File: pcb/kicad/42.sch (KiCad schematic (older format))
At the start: 92 parts, among them J1 USB_C_Receptacle, J2 USB_C_Receptacle, J3 USB_C_Receptacle, K1 KEYSW, K10 KEYSW, K11 KEYSW, K12 KEYSW, K13 KEYSW, K14 KEYSW, K15 KEYSW, K16 KEYSW, K17 KEYSW, K18 KEYSW, K19 KEYSW, K2 KEYSW, K20 KEYSW, K21 KEYSW, K22 KEYSW, K23 KEYSW, K24 KEYSW, K25 KEYSW, K26 KEYSW, K27 KEYSW, K28 KEYSW, K29 KEYSW, K3 KEYSW, K30 KEYSW, K31 KEYSW, K32 KEYSW, K33 KEYSW, K34 KEYSW, K35 KEYSW, K36 KEYSW, K37 KEYSW, K38 KEYSW, K39 KEYSW, K4 KEYSW, K40 KEYSW, K41 KEYSW, K42 KEYSW, K5 KEYSW, K6 KEYSW, K7 KEYSW, K8 KEYSW, K9 KEYSW, U1 TEENSY2.0

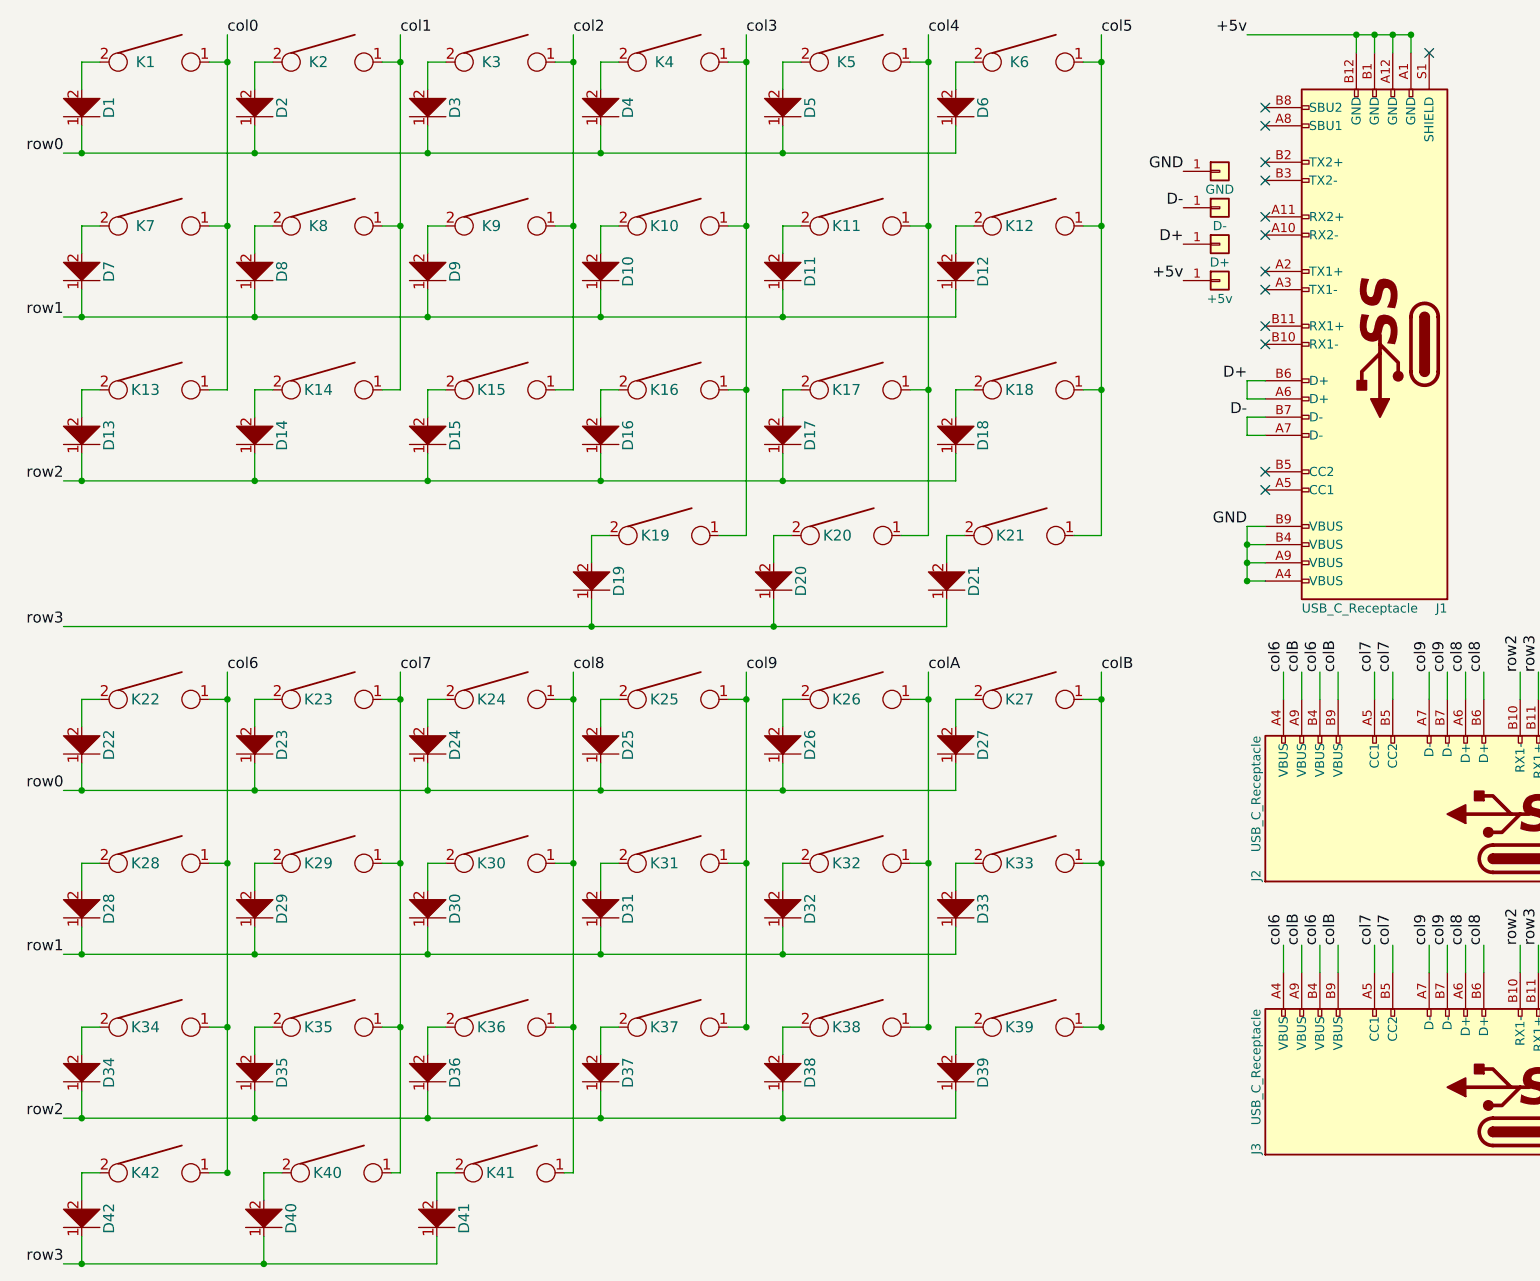
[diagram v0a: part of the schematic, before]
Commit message: fixed inverted connections on USB receptacle
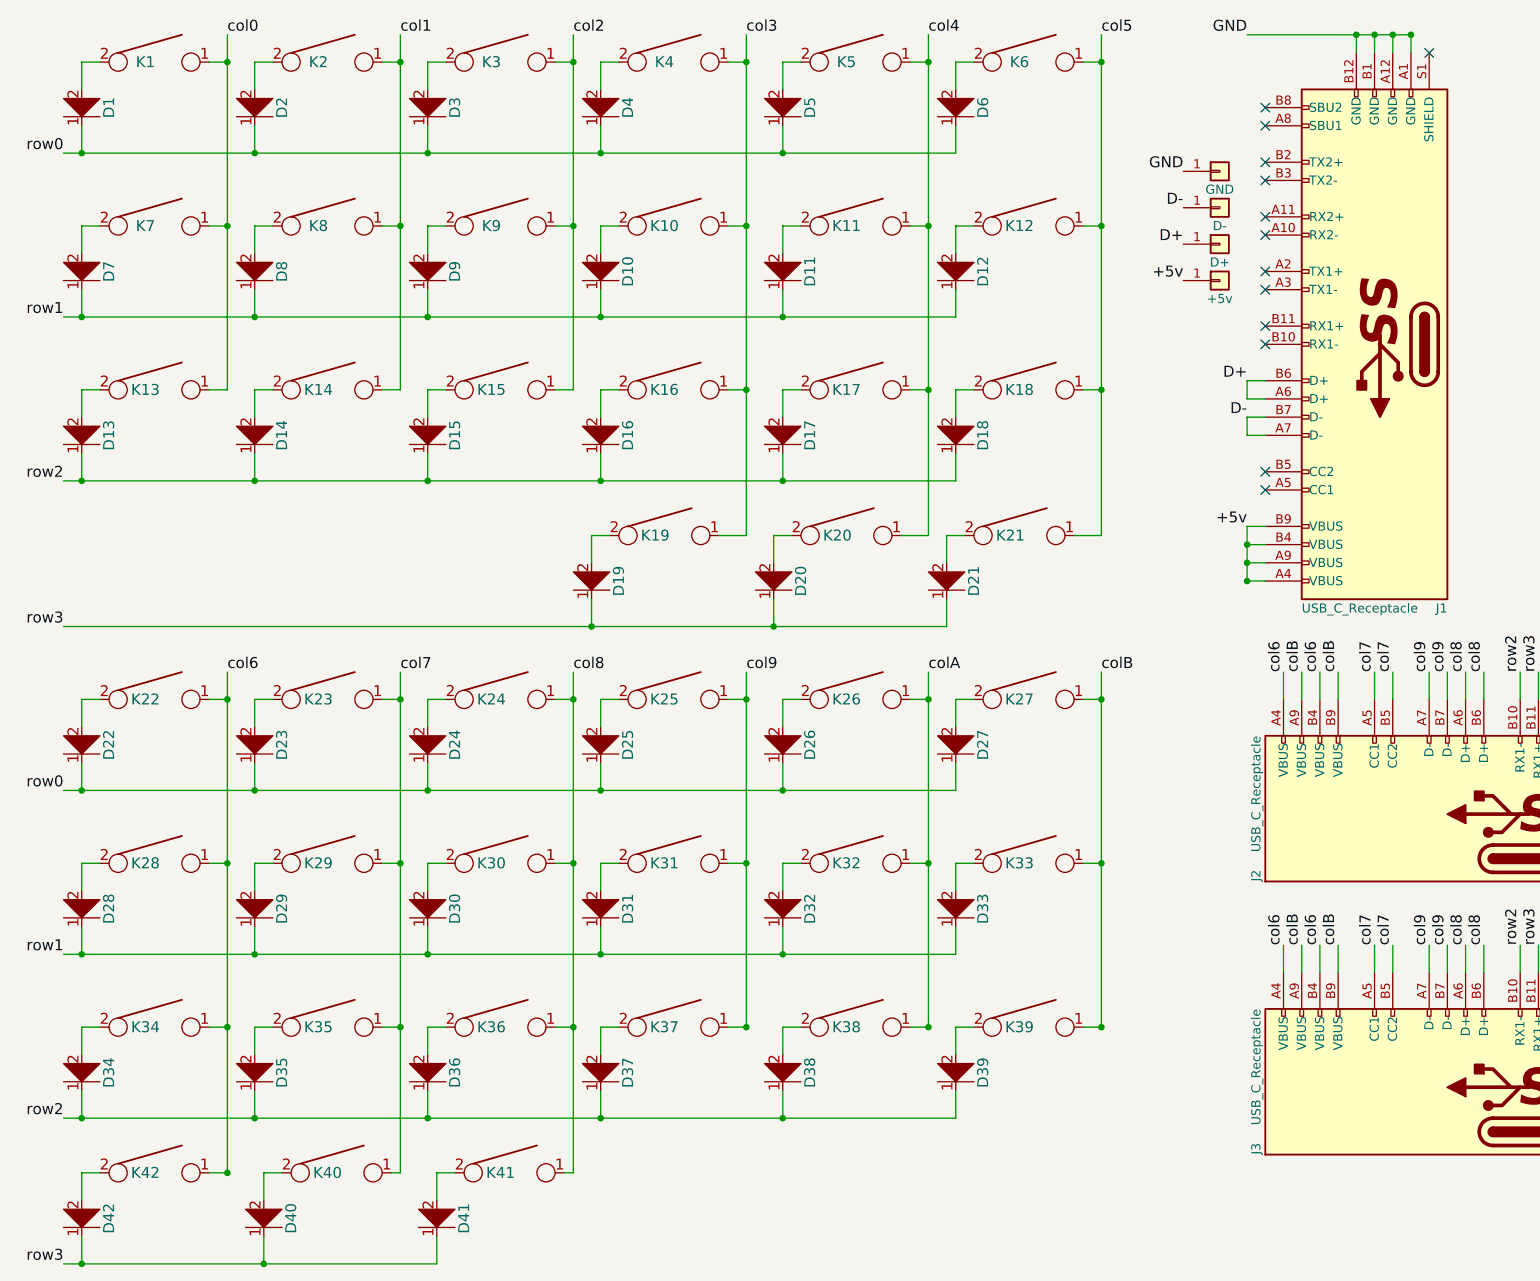
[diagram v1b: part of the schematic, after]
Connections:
- net +5v: now also J1.A4 (VBUS), J1.A9 (VBUS), J1.B4 (VBUS), J1.B9 (VBUS); no longer J1.A1 (GND), J1.A12 (GND), J1.B1 (GND), J1.B12 (GND)
- net GND: now also J1.A1 (GND), J1.A12 (GND), J1.B1 (GND), J1.B12 (GND); no longer J1.A4 (VBUS), J1.A9 (VBUS), J1.B4 (VBUS), J1.B9 (VBUS)
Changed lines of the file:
@@
 EESchema Schematic File Version 2
 LIBS:power
-LIBS:device
-LIBS:switches
-LIBS:relays
-LIBS:motors
-LIBS:transistors
-LIBS:conn
-LIBS:linear
-LIBS:regul
-LIBS:74xx
-LIBS:cmos4000
-LIBS:adc-dac
-LIBS:memory
-LIBS:xilinx
-LIBS:microcontrollers
-LIBS:dsp
-LIBS:microchip
-LIBS:analog_switches
-LIBS:motorola
-LIBS:texas
-LIBS:intel
-LIBS:audio
-LIBS:interface
-LIBS:digital-audio
-LIBS:philips
-LIBS:display
-LIBS:cypress
-LIBS:siliconi
-LIBS:opto
-LIBS:atmel
-LIBS:contrib
-LIBS:valves
-LIBS:42keyboard-cache
+LIBS:42-cache
 EELAYER 25 0
 EELAYER END
@@
 	1050 1250 1050 1400
 Wire Wire Line
-	950  1400 1050 1400
-Wire Wire Line
-	1050 1400 2000 1400
-Wire Wire Line
-	2000 1400 2950 1400
-Wire Wire Line
-	2950 1400 3900 1400
-Wire Wire Line
-	3900 1400 4900 1400
-Wire Wire Line
-	4900 1400 5850 1400
+	950  1400 5850 1400
 Wire Wire Line
 	2000 1400 2000 1250
@@
 	1050 2150 1050 2300
 Wire Wire Line
-	950  2300 1050 2300
-Wire Wire Line
-	1050 2300 2000 2300
-Wire Wire Line
-	2000 2300 2950 2300
-Wire Wire Line
-	2950 2300 3900 2300
-Wire Wire Line
-	3900 2300 4900 2300
-Wire Wire Line
-	4900 2300 5850 2300
+	950  2300 5850 2300
 Wire Wire Line
 	2000 2300 2000 2150
@@
 	1050 3050 1050 3200
 Wire Wire Line
-	950  3200 1050 3200
-Wire Wire Line
-	1050 3200 2000 3200
-Wire Wire Line
-	2000 3200 2950 3200
-Wire Wire Line
-	2950 3200 3900 3200
-Wire Wire Line
-	3900 3200 4900 3200
-Wire Wire Line
-	4900 3200 5850 3200
+	950  3200 5850 3200
 Wire Wire Line
 	2000 3200 2000 3050
@@
 	1750 900  1850 900
 Wire Wire Line
-	1850 750  1850 900
-Wire Wire Line
-	1850 900  1850 1800
-Wire Wire Line
-	1850 1800 1850 2700
+	1850 750  1850 2700
 Wire Wire Line
 	1850 2700 1750 2700
@@
 	2700 900  2800 900
 Wire Wire Line
-	2800 750  2800 900
-Wire Wire Line
-	2800 900  2800 1800
-Wire Wire Line
-	2800 1800 2800 2700
+	2800 750  2800 2700
 Wire Wire Line
 	2800 2700 2700 2700
@@
 	3650 900  3750 900
 Wire Wire Line
-	3750 750  3750 900
-Wire Wire Line
-	3750 900  3750 1800
-Wire Wire Line
-	3750 1800 3750 2700
+	3750 750  3750 2700
 Wire Wire Line
 	3750 2700 3650 2700
@@
 	4600 900  4700 900
 Wire Wire Line
-	4700 750  4700 900
-Wire Wire Line
-	4700 900  4700 1800
-Wire Wire Line
-	4700 1800 4700 2700
-Wire Wire Line
-	4700 2700 4700 3500
+	4700 750  4700 3500
 Wire Wire Line
 	4700 2700 4600 2700
@@
 	5600 900  5700 900
 Wire Wire Line
-	5700 750  5700 900
-Wire Wire Line
-	5700 900  5700 1800
-Wire Wire Line
-	5700 1800 5700 2700
-Wire Wire Line
-	5700 2700 5700 3500
+	5700 750  5700 3500
 Wire Wire Line
 	5700 2700 5600 2700
@@
 	6550 900  6650 900
 Wire Wire Line
-	6650 750  6650 900
-Wire Wire Line
-	6650 900  6650 1800
-Wire Wire Line
-	6650 1800 6650 2700
-Wire Wire Line
-	6650 2700 6650 3500
+	6650 750  6650 3500
 Wire Wire Line
 	6650 2700 6550 2700
@@
 Connection ~ 6650 1800
 Wire Wire Line
-	950  4000 3850 4000
-Wire Wire Line
-	3850 4000 4850 4000
-Wire Wire Line
-	4850 4000 5800 4000
+	950  4000 5800 4000
 Wire Wire Line
 	3950 3500 3850 3500
@@
 	7450 2950 7550 2950
 Wire Wire Line
-	7450 3450 7450 3550
-Wire Wire Line
-	7450 3550 7450 3650
-Wire Wire Line
-	7450 3650 7450 3750
+	7450 3450 7450 3750
 Wire Wire Line
 	7450 3550 7550 3550
@@
 Connection ~ 7450 3650
 Wire Wire Line
-	7450 750  8050 750
-Wire Wire Line
-	8050 750  8150 750
-Wire Wire Line
-	8150 750  8250 750
-Wire Wire Line
-	8250 750  8350 750
+	7450 750  8350 750
 Wire Wire Line
 	8350 750  8350 850
@@
 	1050 4750 1050 4900
 Wire Wire Line
-	950  4900 1050 4900
-Wire Wire Line
-	1050 4900 2000 4900
-Wire Wire Line
-	2000 4900 2950 4900
-Wire Wire Line
-	2950 4900 3900 4900
-Wire Wire Line
-	3900 4900 4900 4900
-Wire Wire Line
-	4900 4900 5850 4900
+	950  4900 5850 4900
 Wire Wire Line
 	2000 4900 2000 4750
@@
 	1050 5650 1050 5800
 Wire Wire Line
-	950  5800 1050 5800
-Wire Wire Line
-	1050 5800 2000 5800
-Wire Wire Line
-	2000 5800 2950 5800
-Wire Wire Line
-	2950 5800 3900 5800
-Wire Wire Line
-	3900 5800 4900 5800
-Wire Wire Line
-	4900 5800 5850 5800
+	950  5800 5850 5800
 Wire Wire Line
 	2000 5800 2000 5650
@@
 	1050 6550 1050 6700
 Wire Wire Line
-	950  6700 1050 6700
-Wire Wire Line
-	1050 6700 2000 6700
-Wire Wire Line
-	2000 6700 2950 6700
-Wire Wire Line
-	2950 6700 3900 6700
-Wire Wire Line
-	3900 6700 4900 6700
-Wire Wire Line
-	4900 6700 5850 6700
+	950  6700 5850 6700
 Wire Wire Line
 	2000 6700 2000 6550
@@
 	1750 4400 1850 4400
 Wire Wire Line
-	1850 4250 1850 4400
-Wire Wire Line
-	1850 4400 1850 5300
-Wire Wire Line
-	1850 5300 1850 6200
-Wire Wire Line
-	1850 6200 1850 7000
+	1850 4250 1850 7000
 Wire Wire Line
 	1850 6200 1750 6200
@@
 	2700 4400 2800 4400
 Wire Wire Line
-	2800 4250 2800 4400
-Wire Wire Line
-	2800 4400 2800 5300
-Wire Wire Line
-	2800 5300 2800 6200
-Wire Wire Line
-	2800 6200 2800 7000
+	2800 4250 2800 7000
 Wire Wire Line
 	2800 6200 2700 6200
@@
 	3650 4400 3750 4400
 Wire Wire Line
-	3750 4250 3750 4400
-Wire Wire Line
-	3750 4400 3750 5300
-Wire Wire Line
-	3750 5300 3750 6200
-Wire Wire Line
-	3750 6200 3750 7000
+	3750 4250 3750 7000
 Wire Wire Line
 	3750 6200 3650 6200
@@
 	4600 4400 4700 4400
 Wire Wire Line
-	4700 4250 4700 4400
-Wire Wire Line
-	4700 4400 4700 5300
-Wire Wire Line
-	4700 5300 4700 6200
+	4700 4250 4700 6200
 Wire Wire Line
 	4700 6200 4600 6200
@@
 	5600 4400 5700 4400
 Wire Wire Line
-	5700 4250 5700 4400
-Wire Wire Line
-	5700 4400 5700 5300
-Wire Wire Line
-	5700 5300 5700 6200
+	5700 4250 5700 6200
 Wire Wire Line
 	5700 6200 5600 6200
@@
 	6550 4400 6650 4400
 Wire Wire Line
-	6650 4250 6650 4400
-Wire Wire Line
-	6650 4400 6650 5300
-Wire Wire Line
-	6650 5300 6650 6200
+	6650 4250 6650 6200
 Wire Wire Line
 	6650 6200 6550 6200
@@
 Connection ~ 1050 6700
 Wire Wire Line
-	950  7500 1050 7500
-Wire Wire Line
-	1050 7500 2050 7500
-Wire Wire Line
-	2050 7500 3000 7500
+	950  7500 3000 7500
 Connection ~ 1850 6200
 Connection ~ 1850 7000
@@
 GND
 Text Label 7450 750  2    60   ~ 0
-+5v
+GND
 Text Label 7450 2650 2    60   ~ 0
 D+
@@
 	7450 2650 7450 2750
 Text Label 7450 3450 2    60   ~ 0
-GND
++5v
 $EndSCHEMATC

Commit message: moved receptacles to the back side, rewired connections
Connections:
- net col6: now also J2.B2 (TX2+), J3.A11 (RX2+); no longer J2.A4 (VBUS), J2.B4 (VBUS), J3.A4 (VBUS), J3.B4 (VBUS)
- net col7: now also J2.B3 (TX2-), J3.A10 (RX2-); no longer J2.A5 (CC1), J2.B5 (CC2), J3.A5 (CC1), J3.B5 (CC2)
- net col8: no longer J2.A6 (D+), J3.A6 (D+)
- net col9: no longer J2.A7 (D-), J3.A7 (D-)
- net colA: now also J2.B10 (RX1-), J3.A3 (TX1-); no longer J2.A8 (SBU1), J2.B8 (SBU2), J3.A8 (SBU1), J3.B8 (SBU2)
- net colB: now also J2.B11 (RX1+), J3.A2 (TX1+); no longer J2.A9 (VBUS), J2.B9 (VBUS), J3.A9 (VBUS), J3.B9 (VBUS)
- net row0: now also J2.A2 (TX1+), J3.B11 (RX1+); no longer J2.A3 (TX1-), J2.B3 (TX2-), J3.A3 (TX1-), J3.B3 (TX2-)
- net row1: now also J2.A3 (TX1-), J3.B10 (RX1-); no longer J2.A2 (TX1+), J2.B2 (TX2+), J3.A2 (TX1+), J3.B2 (TX2+)
- net row2: now also J3.B3 (TX2-); no longer J2.B10 (RX1-), J3.A10 (RX2-), J3.B10 (RX1-)
- net row3: now also J3.B2 (TX2+); no longer J2.B11 (RX1+), J3.A11 (RX2+), J3.B11 (RX1+)
- no-connect marks 38 -> 58
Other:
- moved on the sheet: D22, D23, D24, D25, D26, D27, D28, D29, D30, D31, D32, D33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
